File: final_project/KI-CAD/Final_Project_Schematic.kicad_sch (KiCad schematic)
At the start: 30 parts, among them SW1 Power Button, SW2 RotaryEncoder, SW3 RotaryEncoder, U1 ATmega328P, U2 ESP32-C3-WROOM-02, U3 Bi-Directional Logic Converter, U4 LED MATRIX

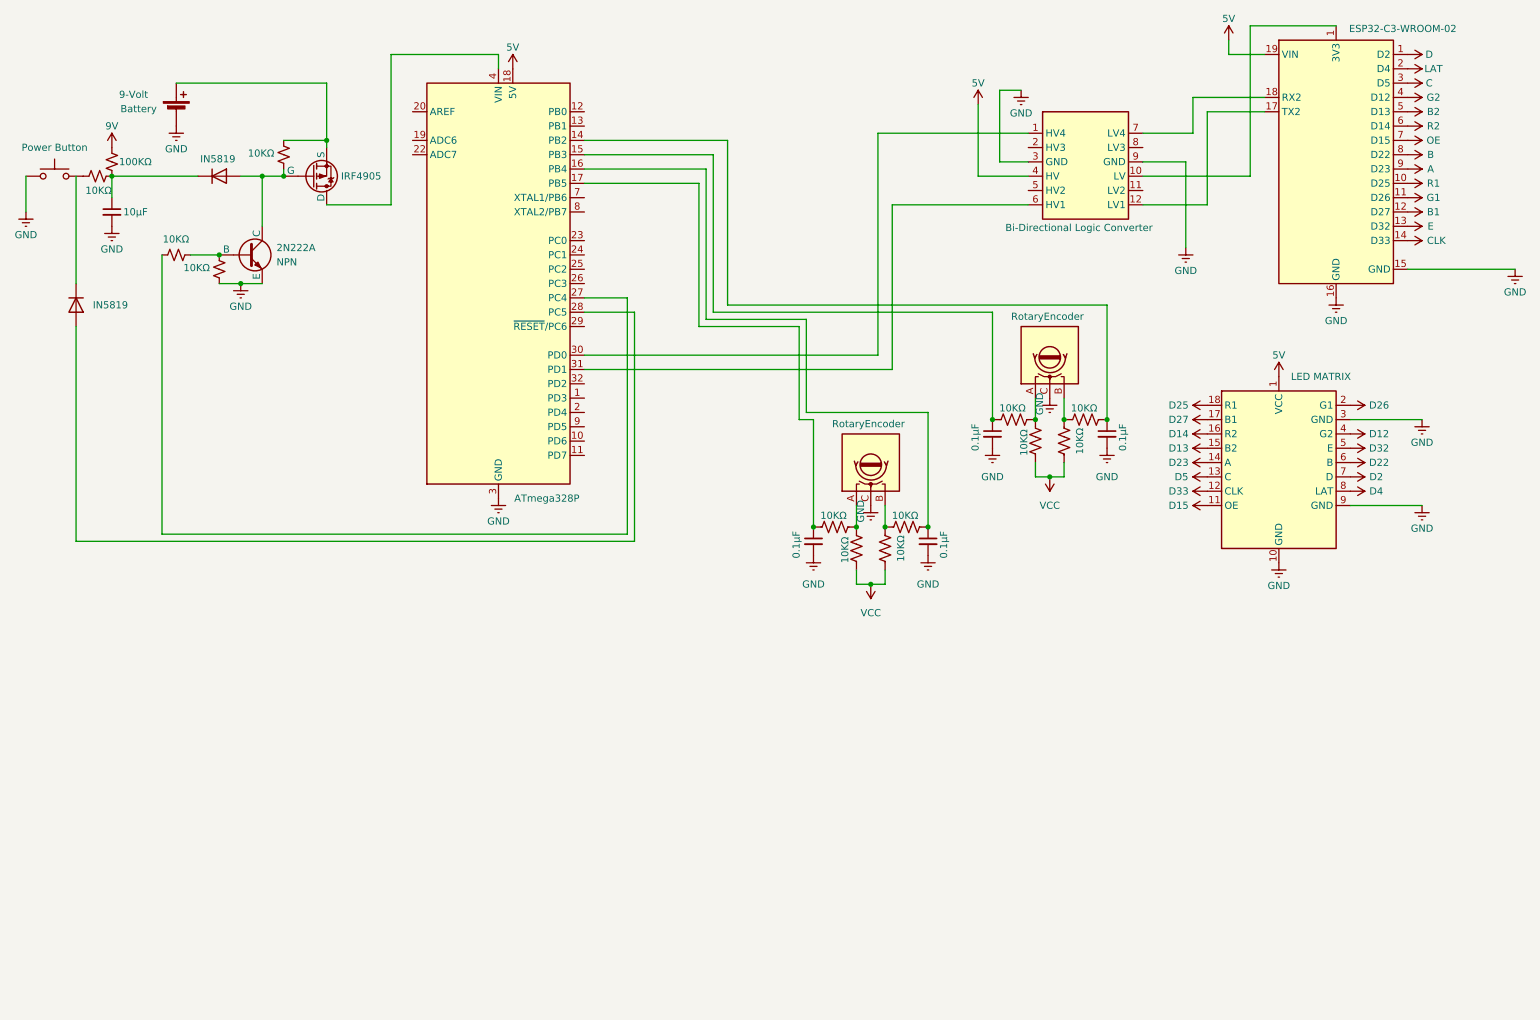
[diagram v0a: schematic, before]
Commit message: Schematic done for now may need changes if we move pins around
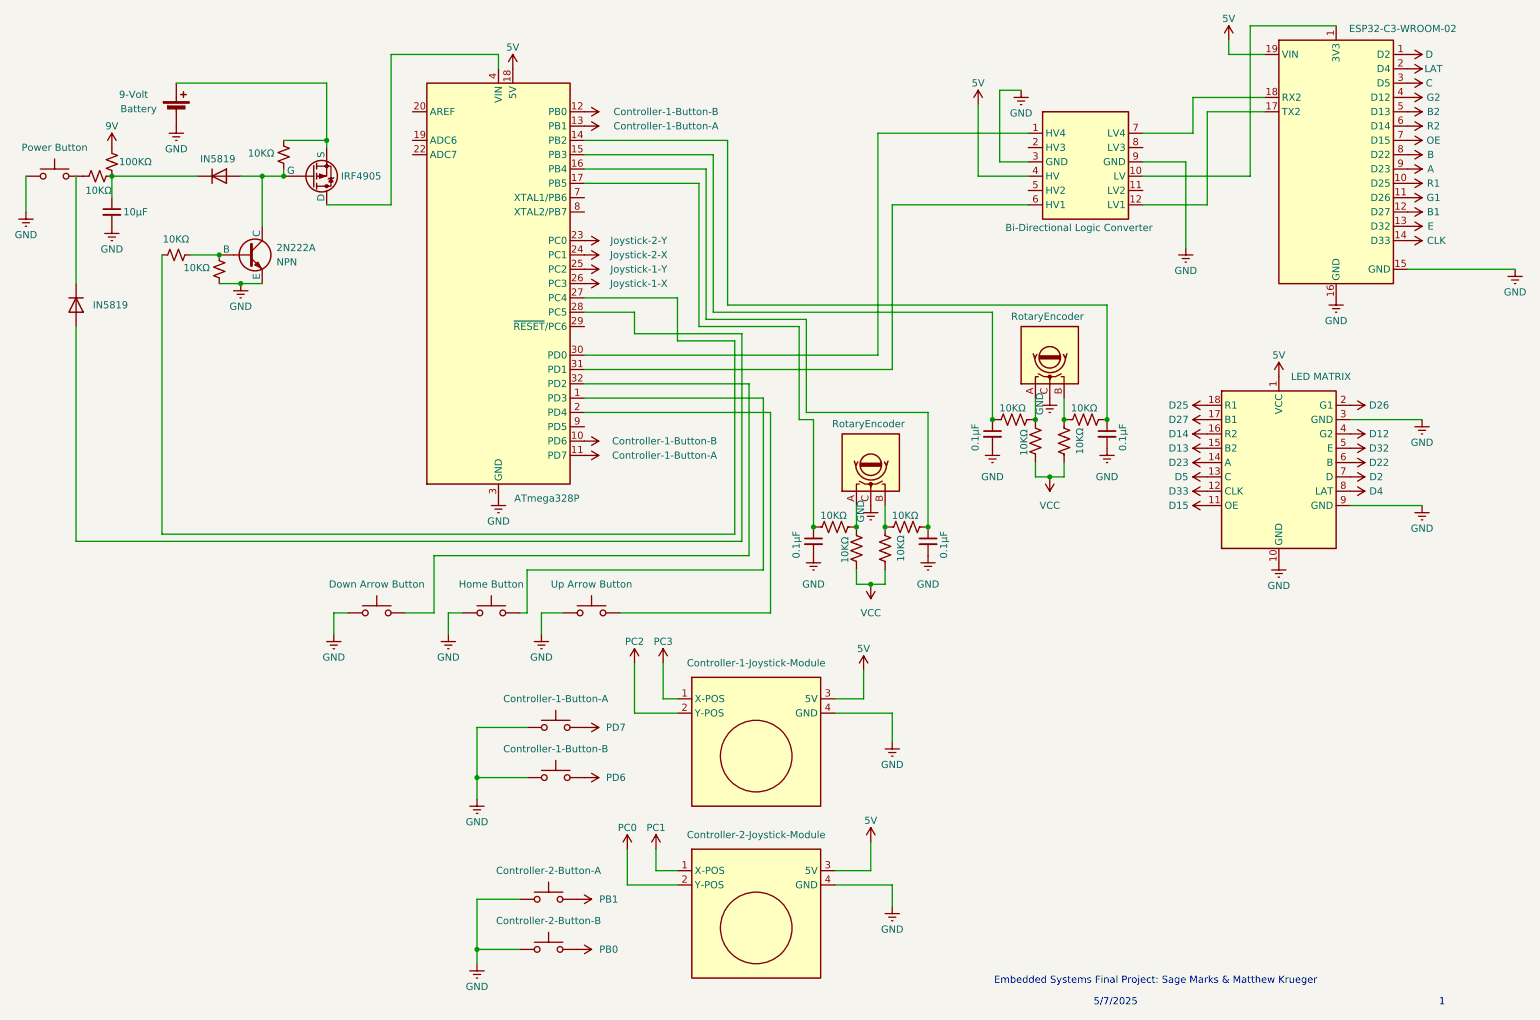
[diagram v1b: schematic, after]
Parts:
- added A1: Controller-1-Joystick-Module, Module:Arduino_Nano, symbol MCU_Module:Arduino_Nano_ESP32
- added A2: Controller-2-Joystick-Module, Module:Arduino_Nano, symbol MCU_Module:Arduino_Nano_ESP32
- added SW10: Controller-2-Button-B, symbol Switch:SW_Push
- added SW4: Home Button, symbol Switch:SW_Push
- added SW5: Up Arrow Button, symbol Switch:SW_Push
- added SW6: Down Arrow Button, symbol Switch:SW_Push
- added SW7: Controller-1-Button-A, symbol Switch:SW_Push
- added SW8: Controller-1-Button-B, symbol Switch:SW_Push
- added SW9: Controller-2-Button-A, symbol Switch:SW_Push
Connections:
- net 5V: now also A1.3 (5V), A2.3 (5V)
- net GND: now also A1.4 (GND), A2.4 (GND), SW10.1, SW4.1, SW5.1, SW6.1, SW7.1, SW8.1, SW9.1
- net at U1.1 (PD3): now also SW4.2
- net Controller-1-Button-B: now reaches U1.10 (PD6)
- net Controller-1-Button-B: now also U1.12 (PB0)
- net Controller-1-Button-A: now reaches U1.11 (PD7)
- net Controller-1-Button-A: now also U1.13 (PB1)
- net at U1.2 (PD4): now also SW5.2
- net Joystick-2-Y: now reaches U1.23 (PC0)
- net Joystick-2-X: now reaches U1.24 (PC1)
- net Joystick-1-Y: now reaches U1.25 (PC2)
- net Joystick-1-X: now reaches U1.26 (PC3)
- net at U1.32 (PD2): now also SW6.2
- new net PB0: SW10.2
- new net PB1: SW9.2
- new net PC0: A2.2 (Y-POS)
- new net PC1: A2.1 (X-POS)
- new net PC2: A1.2 (Y-POS)
- new net PC3: A1.1 (X-POS)
- new net PD6: SW8.2
- new net PD7: SW7.2
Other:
- note added: "1"
- note added: "5/7/2025"
- note added: "Embedded Systems Final Project: Sage Marks & Matthew Krueger"
